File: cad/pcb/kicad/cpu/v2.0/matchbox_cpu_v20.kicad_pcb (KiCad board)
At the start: 6 copper layers, 40 x 66 mm, 83 parts, among them P1 DF12-32-DP, P2 DF12-32-DP, P3 DF12-32-DP, P4 DF12-32-DP, Q1 FDN360P, Q2 FDN360P, SW0 BOOT0, SW1 B3U-3100PM-B, SW2 B3U-3100PM-B, SW3 RESET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

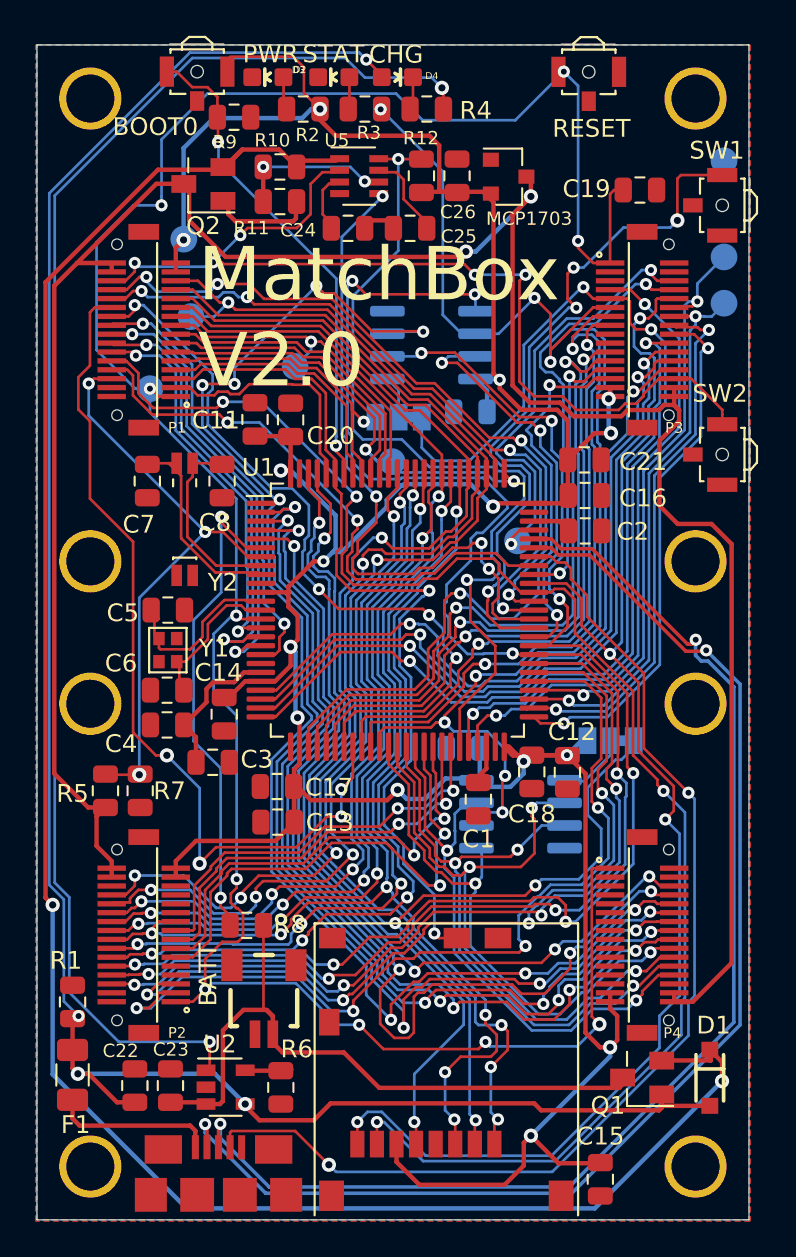
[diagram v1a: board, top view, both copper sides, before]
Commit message: Fix misaligned fill polygons. They now match the cut outline.
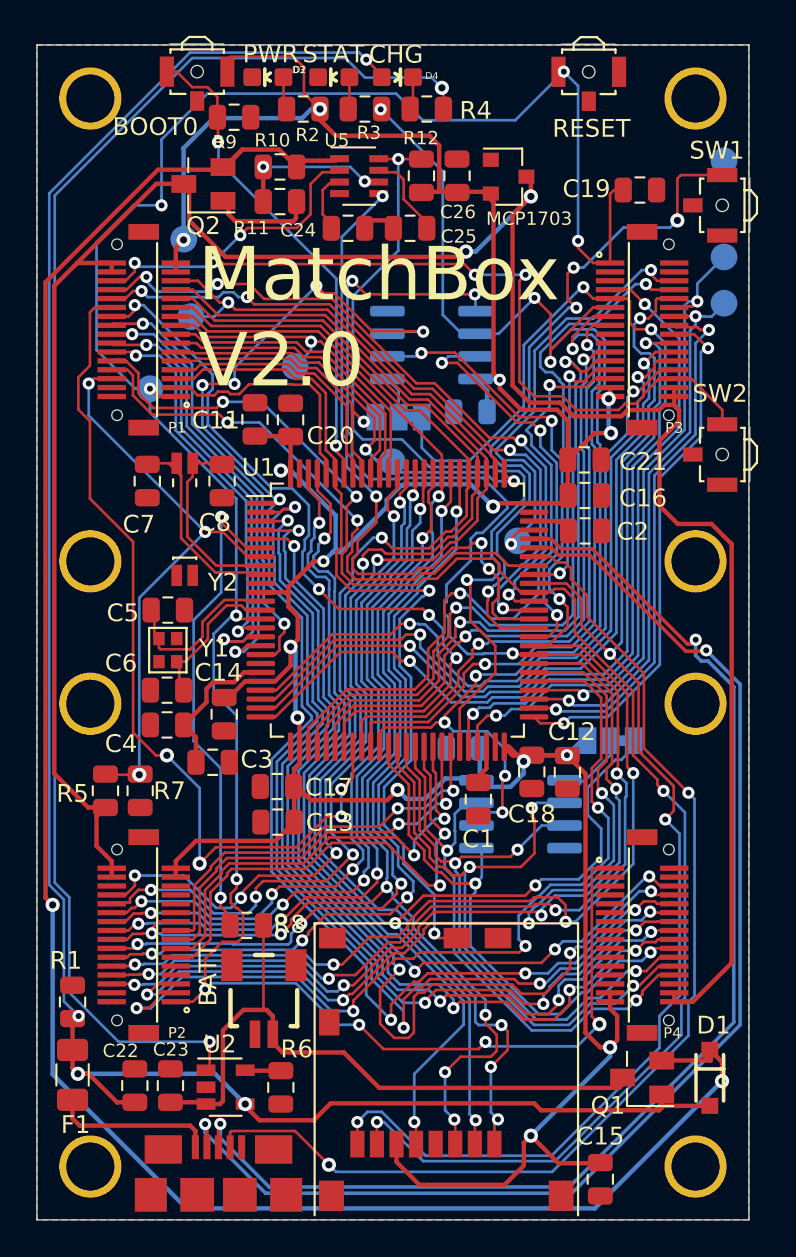
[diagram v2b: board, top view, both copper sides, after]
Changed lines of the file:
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@@
     (polygon
       (pts
-        (xy 40.0773 0.0698) (xy -0.0751 0.0698) (xy -0.0751 -66.01) (xy 40.0773 -66.01)
+        (xy 40 0) (xy 0 0) (xy 0 -66) (xy 40 -66)
       )
     )

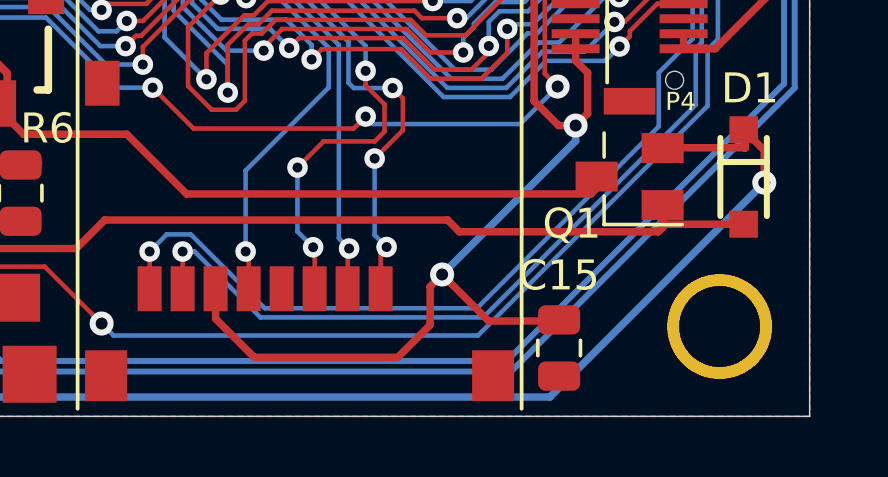
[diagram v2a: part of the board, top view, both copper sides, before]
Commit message: Fix wiring error on SD card (VDD/VSS swapped!)
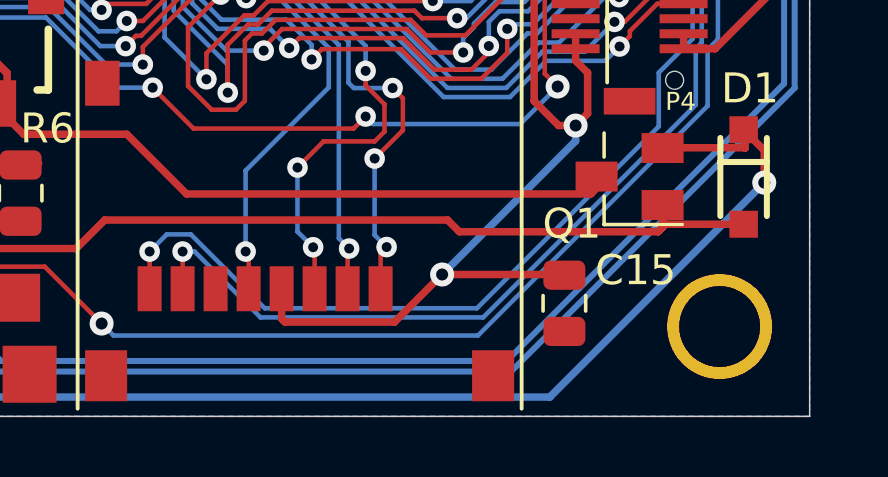
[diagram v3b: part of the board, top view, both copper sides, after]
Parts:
- moved C15 1.50 mm to (31.8, -3.77)
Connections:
- SD1 pad 4: GND -> /VCC_3V3
- SD1 pad 6: /VCC_3V3 -> GND
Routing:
- net /VCC_3V3: track 198.4 -> 194.0 mm
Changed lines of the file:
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@@
     (thickness 1.6)
     (drawings 15)
-    (tracks 2761)
+    (tracks 2760)
     (zones 0)
     (modules 83)
@@
   )
   (setup
-    (last_trace_width 0.1524)
+    (last_trace_width 0.25)
     (user_trace_width 0.1524)
     (user_trace_width 0.254)
@@
       (net 11 /PD2) (solder_mask_margin 0.0762))
     (pad 4 smd rect (at 0.6 3.75 180) (size 0.8 1.5) (layers Top F.Paste F.Mask)
-      (net 1 GND) (solder_mask_margin 0.0762))
+      (net 2 /VCC_3V3) (solder_mask_margin 0.0762))
     (pad 5 smd rect (at 1.7 3.75 180) (size 0.8 1.5) (layers Top F.Paste F.Mask)
       (net 12 /PC12) (solder_mask_margin 0.0762))
     (pad 6 smd rect (at 2.8 3.75 180) (size 0.8 1.5) (layers Top F.Paste F.Mask)
-      (net 2 /VCC_3V3) (solder_mask_margin 0.0762))
+      (net 1 GND) (solder_mask_margin 0.0762))
     (pad 7 smd rect (at 3.9 3.75 180) (size 0.8 1.5) (layers Top F.Paste F.Mask)
       (net 21 /PC8) (solder_mask_margin 0.0762))
@@
   )
   (module Capacitor_SMD:C_0805_2012Metric (layer Top)
-    (at 31.65 -2.285 270)
+    (at 31.825 -3.775 270)
     (descr "Capacitor SMD 0805 (2012 Metric), square (rectangular) end terminal, IPC_7351 nominal, (Body size source: https://docs.google.com/spreadsheets/d/1BsfQQcO9C6DZCsRaXUlFlo91Tg2WpOkGARC1WS5S8t0/edit?usp=sharing), generated with kicad-footprint-generator")
     (tags capacitor)
     (attr smd)
-    (fp_text reference C15 (at -2.415 0 180) (layer F.SilkS)
+    (fp_text reference C15 (at -1.1 -2.375 180) (layer F.SilkS)
       (effects (font (size 1 1) (thickness 0.15)))
     )
@@
   (segment (start 7.8001 -19.26) (end 7.8001 -19.76) (width 0.25) (layer Top) (net 2) (status 30))
   (segment (start 32.1999 -12.26) (end 32.1999 -12.76) (width 0.25) (layer Top) (net 2) (status 30))
-  (segment (start 29.3 -3.185) (end 27.75 -4.735) (width 0.25) (layer Top) (net 2))
-  (segment (start 31.65 -3.185) (end 29.3 -3.185) (width 0.25) (layer Top) (net 2) (status 10))
   (via (at 27.75 -4.735) (size 0.8) (drill 0.4) (layers Top Bottom) (net 2))
   (segment (start 7.8001 -54.619623) (end 8.237319 -55.056842) (width 0.25) (layer Top) (net 2))
@@
   (segment (start 12.575 -35.26) (end 14.128048 -35.26) (width 0.25) (layer Top) (net 2) (status 10))
   (segment (start 14.4575 -24.51) (end 14.4575 -22.35) (width 0.25) (layer Top) (net 2) (status 30))
-  (segment (start 27.350001 -4.335001) (end 27.75 -4.735) (width 0.25) (layer Top) (net 2))
-  (segment (start 27.350001 -3.050001) (end 27.350001 -4.335001) (width 0.25) (layer Top) (net 2))
-  (segment (start 26.272598 -1.972598) (end 27.350001 -3.050001) (width 0.25) (layer Top) (net 2))
-  (segment (start 20.2 -3.26) (end 21.487402 -1.972598) (width 0.25) (layer Top) (net 2))
-  (segment (start 21.487402 -1.972598) (end 26.272598 -1.972598) (width 0.25) (layer Top) (net 2))
-  (segment (start 20.2 -4.26) (end 20.2 -3.26) (width 0.25) (layer Top) (net 2) (status 10))
   (via (at 32.2 -9.7) (size 0.8) (drill 0.4) (layers Top Bottom) (net 2))
   (segment (start 27.75 -4.735) (end 32.2 -9.185) (width 0.25) (layer Bottom) (net 2))
@@
   (segment (start 14.128048 -34.446952) (end 14.649999 -33.925001) (width 0.25) (layer Top) (net 2))
   (segment (start 14.128048 -35.26) (end 14.128048 -34.446952) (width 0.25) (layer Top) (net 2))
+  (segment (start 22.4 -3.26) (end 22.4 -4.26) (width 0.25) (layer Top) (net 2))
+  (segment (start 22.51 -3.15) (end 22.4 -3.26) (width 0.25) (layer Top) (net 2))
+  (segment (start 26.165 -3.15) (end 22.51 -3.15) (width 0.25) (layer Top) (net 2))
+  (segment (start 27.75 -4.735) (end 26.165 -3.15) (width 0.25) (layer Top) (net 2))
+  (segment (start 27.76 -4.725) (end 27.75 -4.735) (width 0.25) (layer Top) (net 2))
+  (segment (start 31.8025 -4.735) (end 31.825 -4.7125) (width 0.25) (layer Top) (net 2))
+  (segment (start 27.75 -4.735) (end 31.8025 -4.735) (width 0.25) (layer Top) (net 2))
   (segment (start 15.9 -43.085) (end 16.25 -42.735) (width 0.1524) (layer Top) (net 3) (status 20))
   (segment (start 11.366427 -46.394445) (end 11.921238 -46.949256) (width 0.1524) (layer Top) (net 3))

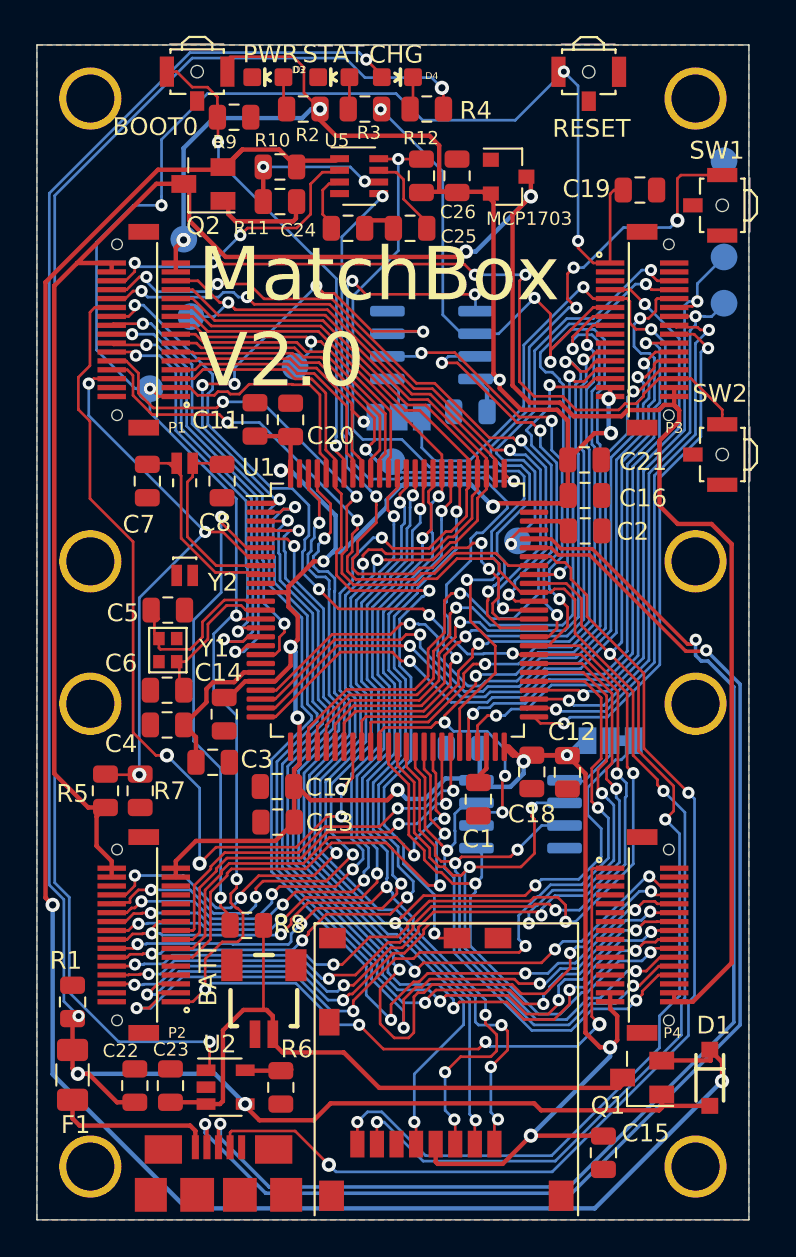
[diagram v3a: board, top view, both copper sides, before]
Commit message: Tune ground plane around SD card
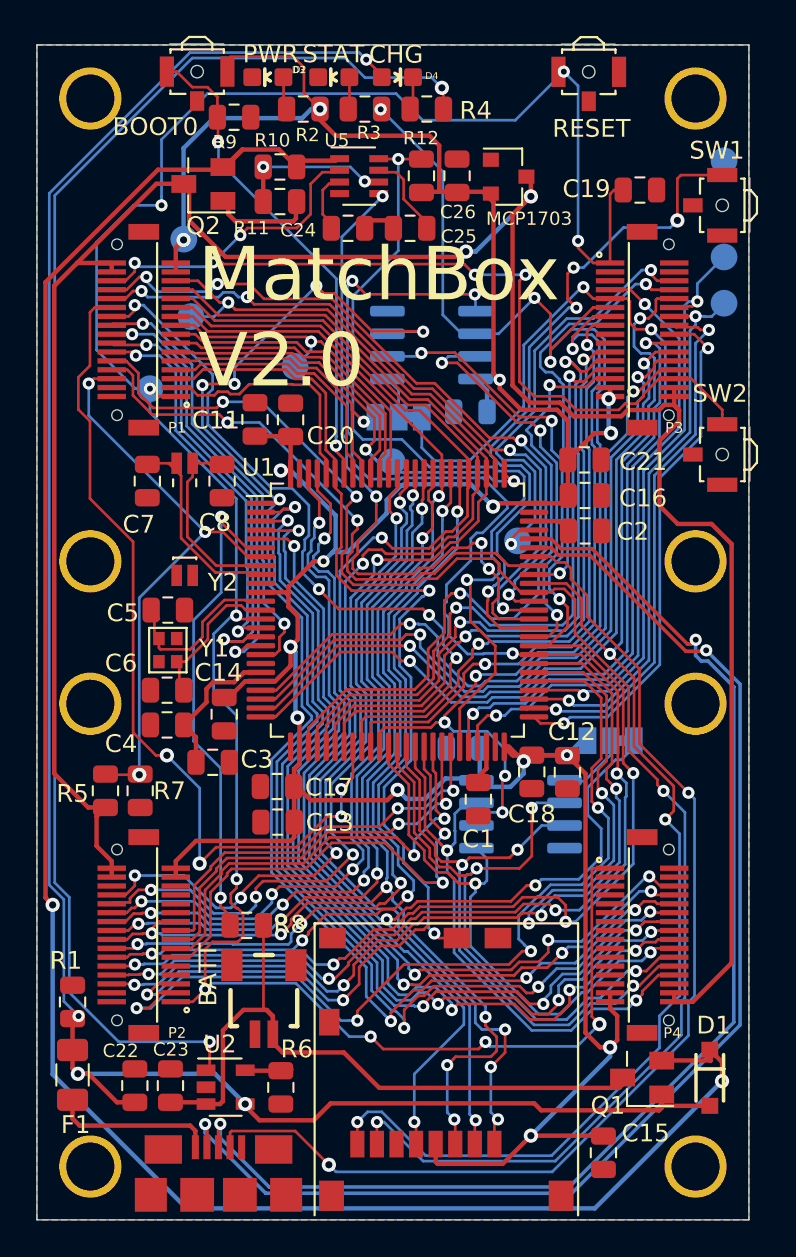
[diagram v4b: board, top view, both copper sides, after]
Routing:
- net /PE1: track 58.6 -> 51.4 mm
- net /PD8: track 50.0 -> 51.0 mm
- net /PE5: track 52.0 -> 52.7 mm
- net /VCC_3V3: track 194.0 -> 194.7 mm
- net /PE0: track 50.3 -> 51.0 mm
- net /PE6: track 50.1 -> 50.8 mm
- net /PE7: track 31.1 -> 31.6 mm

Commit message: Minor cleanup before sending out for fab - Replace STM32H743VI with STM32H753VI which is currently easier to get - Fix mislabeled CN1 issue (now called BATT1) - Fix mislabeled wires on STM part for 16MHz oscillator
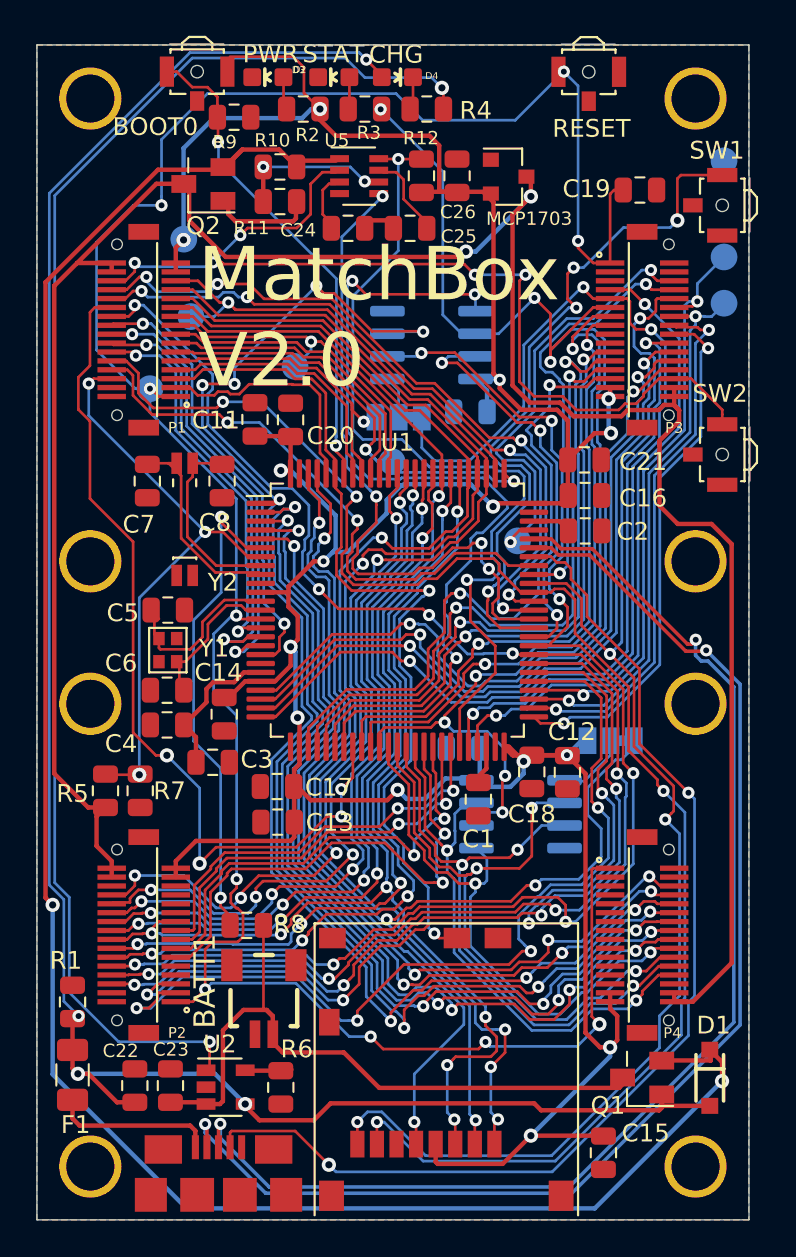
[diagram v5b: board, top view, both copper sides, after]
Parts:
- removed BATT: ?M02B-SRSS-TBS, matchbox_cpu_v20:SM02B-SRSS-TB
- added BATT1: SM02B-SRSS-TBS, matchbox_cpu_v20:SM02B-SRSS-TB, F.Cu at (12.8, -13.4)
- U1: value STM32H743VG -> STM32H753VITx
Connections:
- C5 pad 1: /OSC_OUT -> /OSC_IN
- C6 pad 1: /OSC_IN -> /OSC_OUT
- U1 pad 12: /OSC_OUT -> /OSC_IN
- U1 pad 13: /OSC_IN -> /OSC_OUT
- Y1 pad 1: /OSC_OUT -> /OSC_IN
- Y1 pad 3: /OSC_IN -> /OSC_OUT
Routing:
- net /OSC_OUT: track 10.1 -> 8.40 mm
- net /OSC_IN: track 8.40 -> 10.1 mm

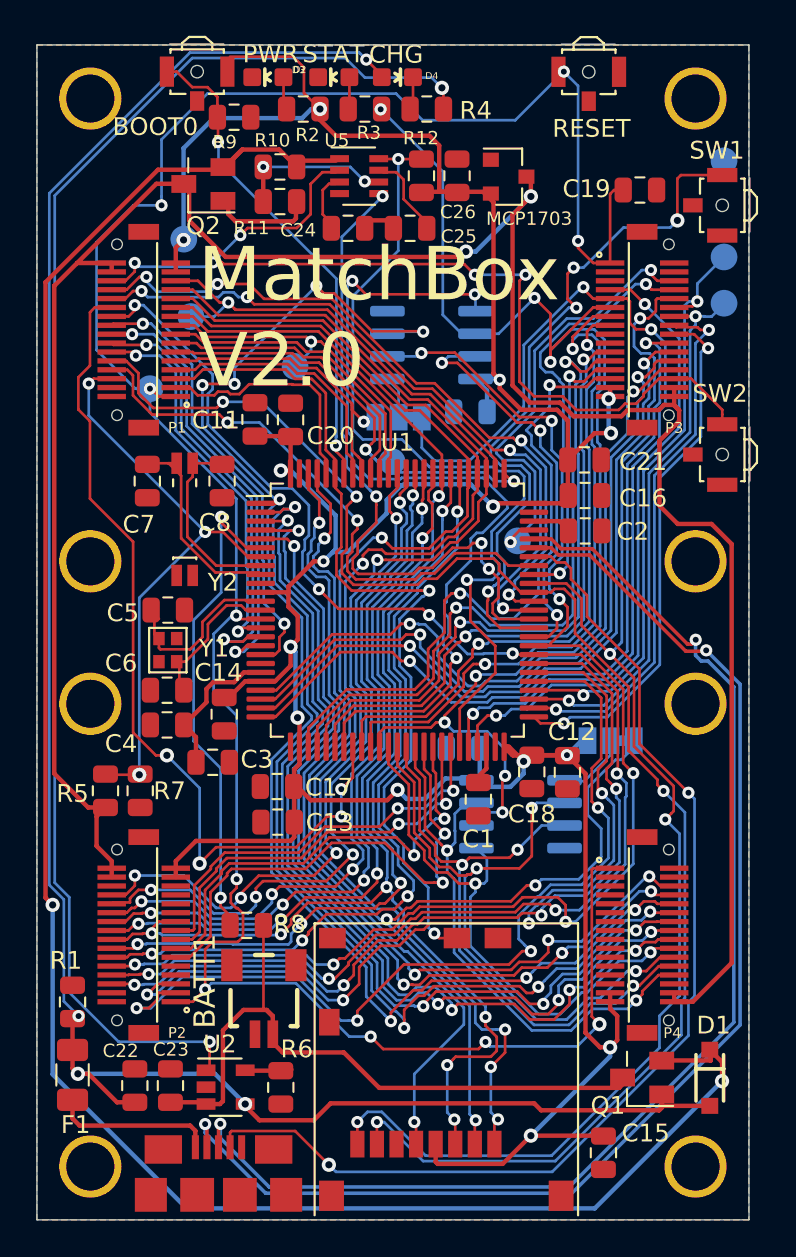
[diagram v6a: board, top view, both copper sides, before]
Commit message: Fix footprint issues on P1, P2 and P3 as well as CPU
After uploading, I noticed some traces would hang off the respective
pads, which will make soldering error-prone on these parts. Too late
for this batch, maybe next.
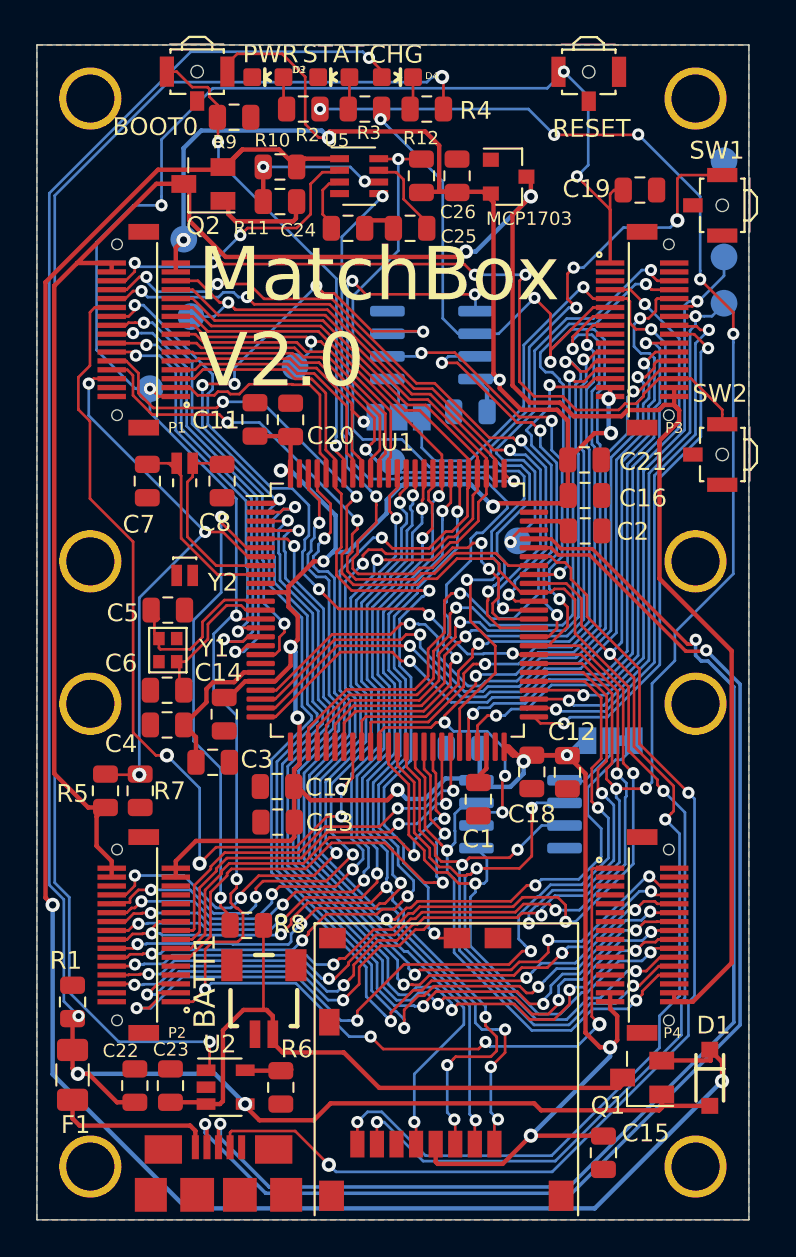
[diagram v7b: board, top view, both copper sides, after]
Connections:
- R2 pad 2: /VCC_3V3 -> /PD10
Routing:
- net /PD10: track 48.2 -> 109.4 mm, vias 4 -> 10
- net /VCC_3V3: track 194.7 -> 196.6 mm
- net /RESET#: track 140.3 -> 139.0 mm
- net /VCC: track 134.7 -> 133.5 mm
- net /STAT: track 82.6 -> 82.1 mm
